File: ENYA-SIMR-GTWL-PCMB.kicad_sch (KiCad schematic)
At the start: 0 parts

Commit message: schematic + PCB done. ready to tag and order
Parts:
- added FID1, FID2, FID3, FID5, FID6, FID7: Fiducial, ENYA_Mechanical:Fiducial_1.5mm_Mask3mm, symbol ENYA_Mechanical:Fiducial
- added G1: Electronya_Logo, ENYA_Bitmap:Electronya_Logo_12MM, symbol ENYA_Bitmap:Electronya_Logo
- added G2: CC-BY-SA_Logo, ENYA_Bitmap:CC-BY-SA_10MM, symbol ENYA_Bitmap:CC-BY-SA_Logo
- added MH1, MH2, MH3, MH4: MH-NPLTD-M3, MountingHole:MountingHole_3.2mm_M3_DIN965, symbol ENYA_Mechanical:MH-NPLTD-M3
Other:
- added sheet BUTTONS_ENCODERS_LEDS (ENYA-SIMR-GTWL-PCMB_BTN_ENC_LED.kicad_sch)
- added sheet MCU (ENYA-SIMR-GTWL-PCMB_MCU.kicad_sch)
- added sheet USB_PWR (ENYA-SIMR-GTWL-PCMB_USB_PWR.kicad_sch)
- company: (none) -> Electronya
- title: (none) -> DIY GT Wheel Main Board

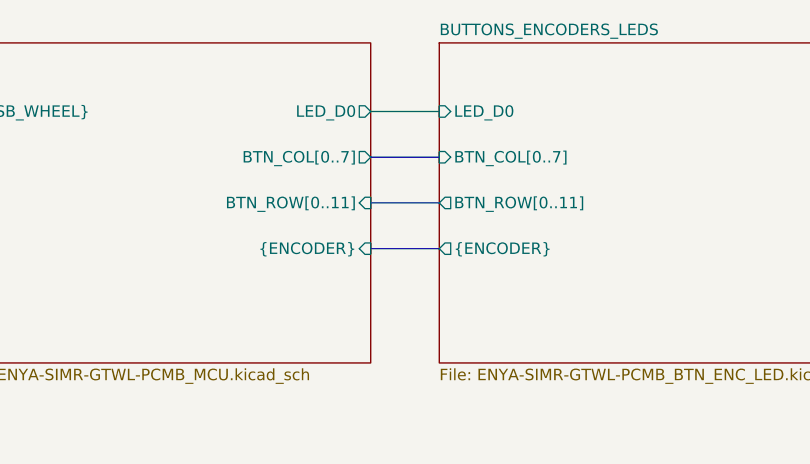
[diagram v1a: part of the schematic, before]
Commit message: rework for encoder instead of selector switch
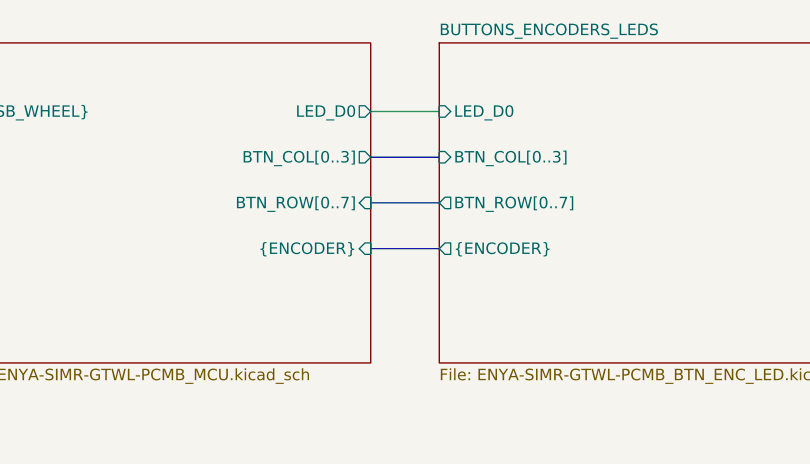
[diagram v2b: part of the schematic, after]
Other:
- sheet BUTTONS_ENCODERS_LEDS ports: added BTN_COL[0..3], BTN_ROW[0..7]; removed BTN_COL[0..7], BTN_ROW[0..11]
- sheet MCU ports: added BTN_COL[0..3], BTN_ROW[0..7]; removed BTN_COL[0..7], BTN_ROW[0..11]
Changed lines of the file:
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@@
       (effects (font (size 1.27 1.27)) (justify right))
     )
-    (pin "BTN_COL[0..7]" output (at 238.76 124.46 0)
+    (pin "BTN_COL[0..3]" output (at 238.76 124.46 0)
       (effects (font (size 1.27 1.27)) (justify right))
     )
-    (pin "BTN_ROW[0..11]" input (at 238.76 129.54 0)
+    (pin "BTN_ROW[0..7]" input (at 238.76 129.54 0)
       (effects (font (size 1.27 1.27)) (justify right))
     )
@@
       (effects (font (size 1.27 1.27)) (justify left top))
     )
-    (pin "BTN_ROW[0..11]" output (at 246.38 129.54 180)
+    (pin "BTN_ROW[0..7]" output (at 246.38 129.54 180)
       (effects (font (size 1.27 1.27)) (justify left))
     )
-    (pin "BTN_COL[0..7]" input (at 246.38 124.46 180)
+    (pin "BTN_COL[0..3]" input (at 246.38 124.46 180)
       (effects (font (size 1.27 1.27)) (justify left))
     )
